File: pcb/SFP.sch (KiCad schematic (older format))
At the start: 13 parts

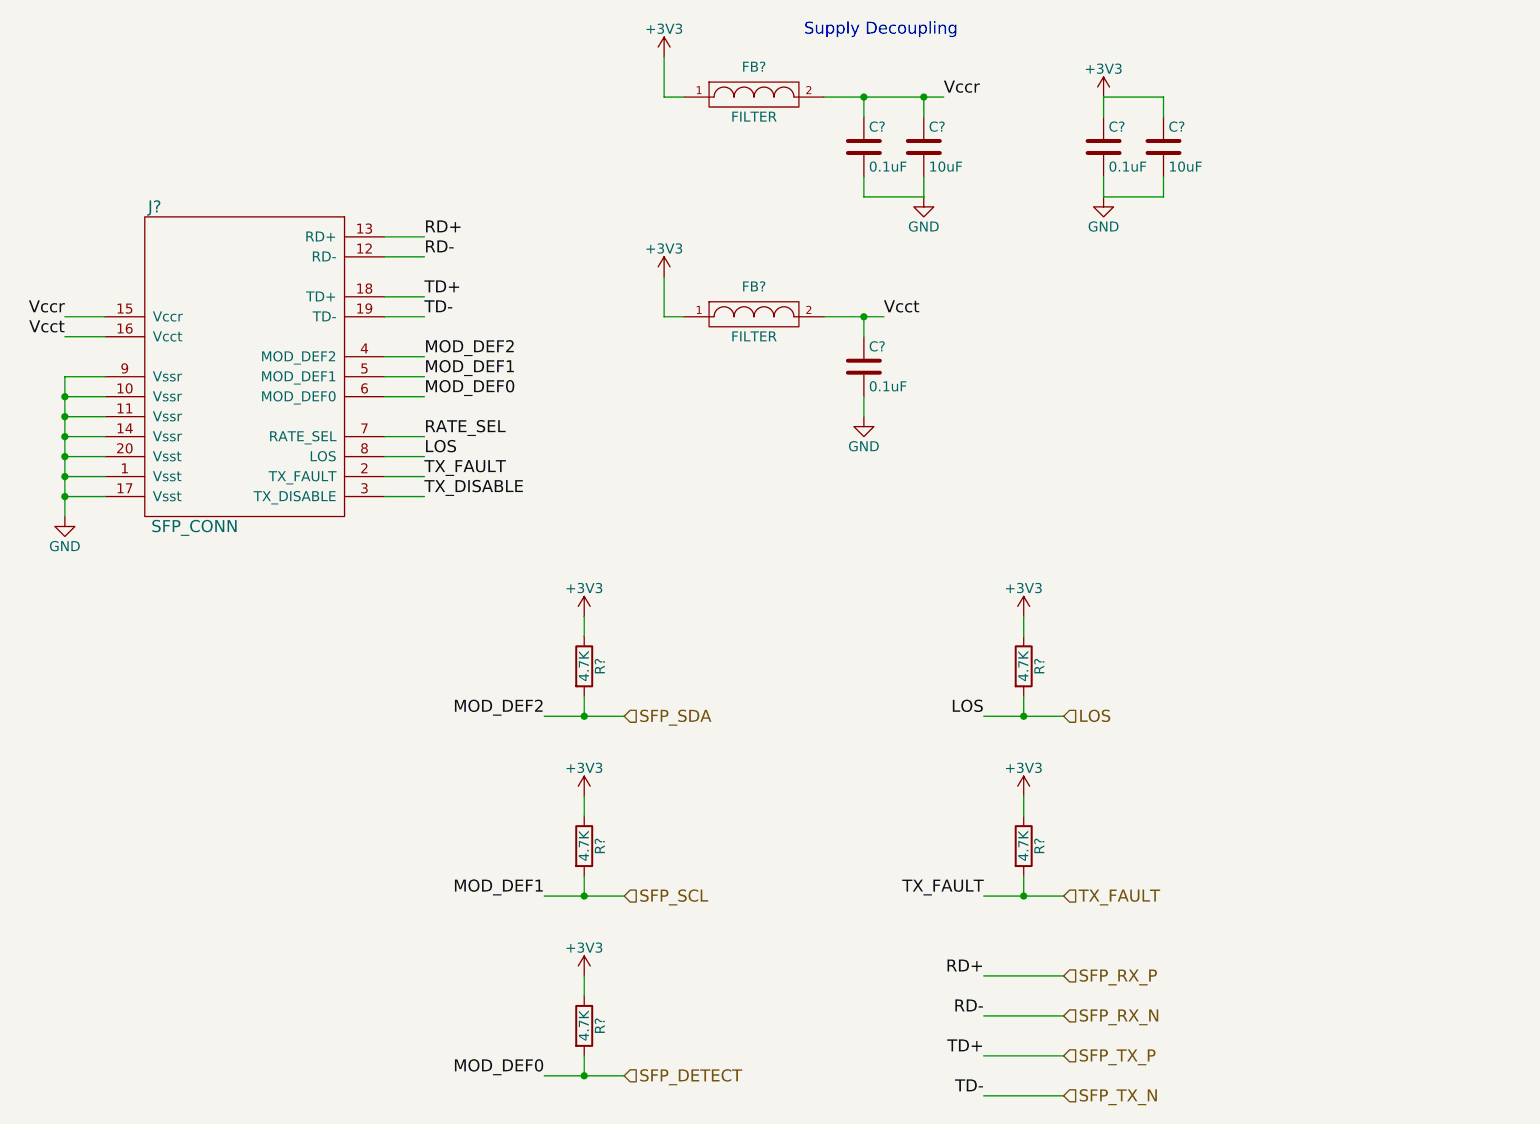
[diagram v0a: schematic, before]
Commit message: Added part numbers and updated schematic
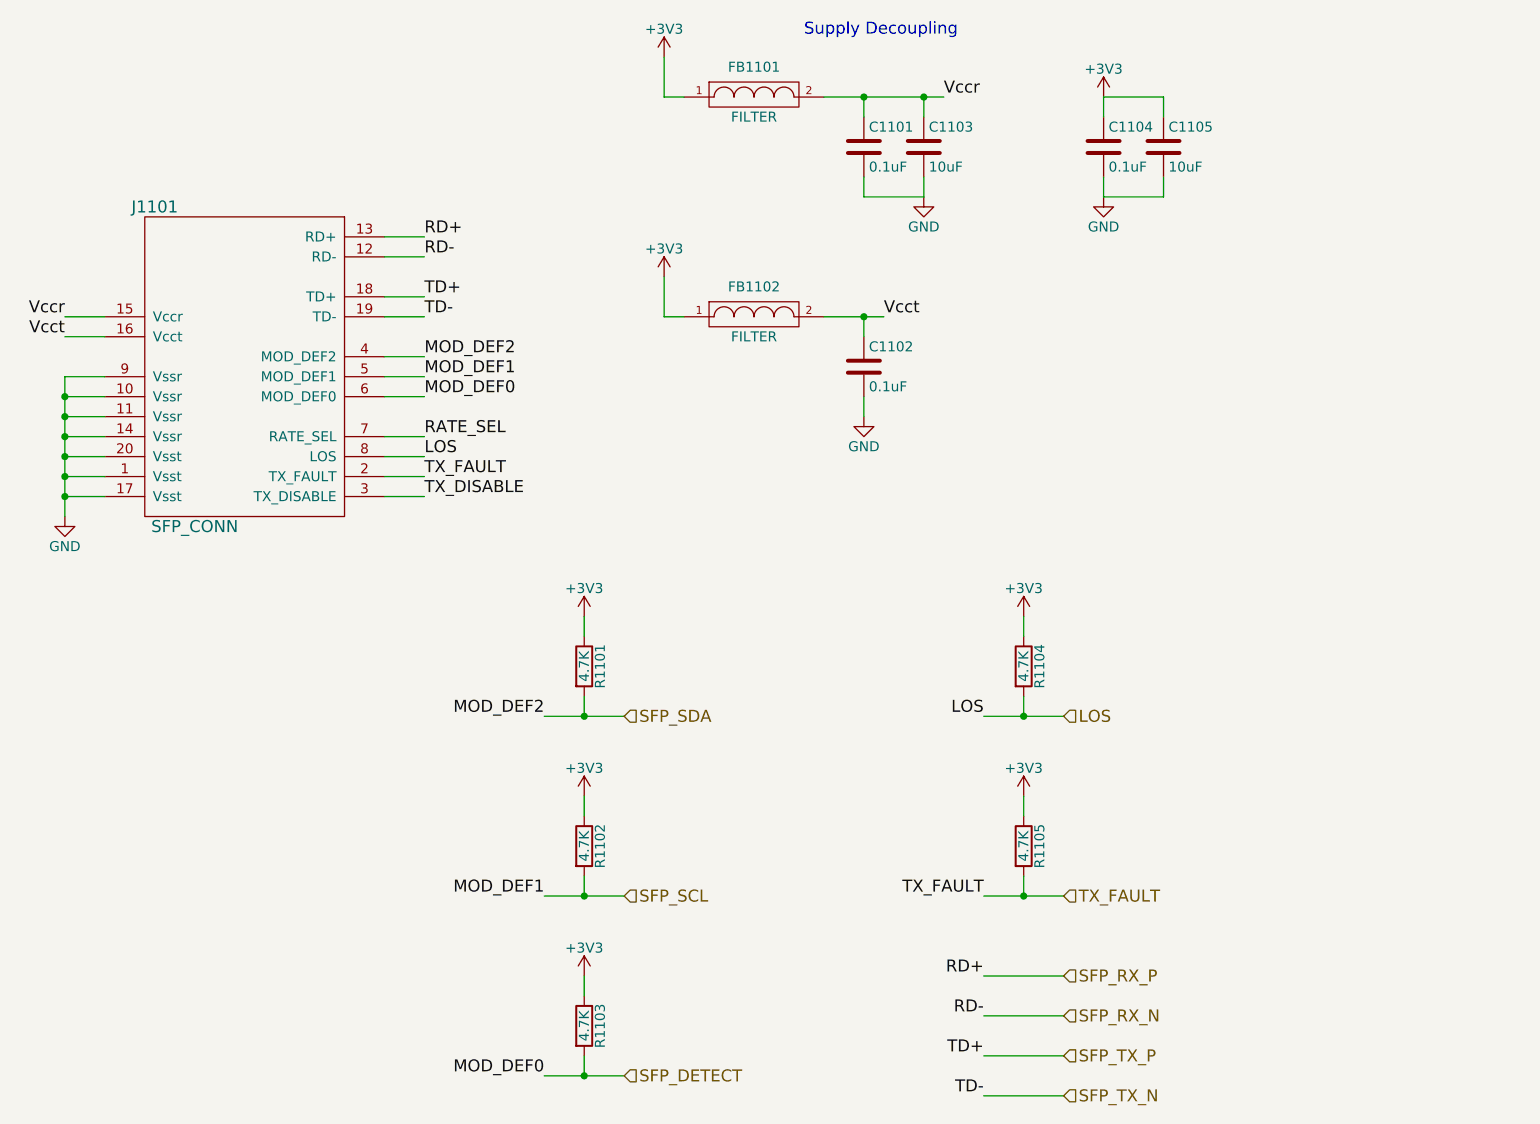
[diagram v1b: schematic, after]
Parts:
- gave numbers to parts that had none: 13
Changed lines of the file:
@@
 $EndDescr
 $Comp
-L SFP_CONN J?
+L SFP_CONN J1101
 U 1 1 56515F52
 P 3600 2350
-F 0 "J?" H 3150 3150 60  0000 C CNN
+F 0 "J1101" H 3150 3150 60  0000 C CNN
 F 1 "SFP_CONN" H 3350 1550 60  0000 C CNN
 F 2 "" H 5000 3150 60  0000 C CNN
@@
 $EndComp
 $Comp
-L GND #PWR?
+L GND #PWR1101
 U 1 1 56515F98
 P 2700 3100
-F 0 "#PWR?" H 2700 2850 50  0001 C CNN
+F 0 "#PWR1101" H 2700 2850 50  0001 C CNN
 F 1 "GND" H 2700 2950 50  0000 C CNN
 F 2 "" H 2700 3100 60  0000 C CNN
@@
 $EndComp
 $Comp
-L +3V3 #PWR?
+L +3V3 #PWR1111
 U 1 1 56515FAF
 P 7900 1000
-F 0 "#PWR?" H 7900 850 50  0001 C CNN
+F 0 "#PWR1111" H 7900 850 50  0001 C CNN
 F 1 "+3V3" H 7900 1140 50  0000 C CNN
 F 2 "" H 7900 1000 60  0000 C CNN
@@
 $EndComp
 $Comp
-L GND #PWR?
+L GND #PWR1112
 U 1 1 56515FCB
 P 7900 1500
-F 0 "#PWR?" H 7900 1250 50  0001 C CNN
+F 0 "#PWR1112" H 7900 1250 50  0001 C CNN
 F 1 "GND" H 7900 1350 50  0000 C CNN
 F 2 "" H 7900 1500 60  0000 C CNN
@@
 $EndComp
 $Comp
-L C C?
+L C C1104
 U 1 1 56515FE4
 P 7900 1250
-F 0 "C?" H 7925 1350 50  0000 L CNN
+F 0 "C1104" H 7925 1350 50  0000 L CNN
 F 1 "0.1uF" H 7925 1150 50  0000 L CNN
 F 2 "" H 7938 1100 30  0000 C CNN
@@
 $EndComp
 $Comp
-L C C?
+L C C1105
 U 1 1 5651600E
 P 8200 1250
-F 0 "C?" H 8225 1350 50  0000 L CNN
+F 0 "C1105" H 8225 1350 50  0000 L CNN
 F 1 "10uF" H 8225 1150 50  0000 L CNN
 F 2 "" H 8238 1100 30  0000 C CNN
@@
 $EndComp
 $Comp
-L C C?
+L C C1103
 U 1 1 56516041
 P 7000 1250
-F 0 "C?" H 7025 1350 50  0000 L CNN
+F 0 "C1103" H 7025 1350 50  0000 L CNN
 F 1 "10uF" H 7025 1150 50  0000 L CNN
 F 2 "" H 7038 1100 30  0000 C CNN
@@
 $EndComp
 $Comp
-L C C?
+L C C1101
 U 1 1 56516075
 P 6700 1250
-F 0 "C?" H 6725 1350 50  0000 L CNN
+F 0 "C1101" H 6725 1350 50  0000 L CNN
 F 1 "0.1uF" H 6725 1150 50  0000 L CNN
 F 2 "" H 6738 1100 30  0000 C CNN
@@
 $EndComp
 $Comp
-L C C?
+L C C1102
 U 1 1 5651609E
 P 6700 2350
-F 0 "C?" H 6725 2450 50  0000 L CNN
+F 0 "C1102" H 6725 2450 50  0000 L CNN
 F 1 "0.1uF" H 6725 2250 50  0000 L CNN
 F 2 "" H 6738 2200 30  0000 C CNN
@@
 $EndComp
 $Comp
-L FILTER FB?
+L FILTER FB1101
 U 1 1 565160D3
 P 6150 1000
-F 0 "FB?" H 6150 1150 50  0000 C CNN
+F 0 "FB1101" H 6150 1150 50  0000 C CNN
 F 1 "FILTER" H 6150 900 50  0000 C CNN
 F 2 "" H 6150 1000 60  0000 C CNN
@@
 $EndComp
 $Comp
-L FILTER FB?
+L FILTER FB1102
 U 1 1 5651610E
 P 6150 2100
-F 0 "FB?" H 6150 2250 50  0000 C CNN
+F 0 "FB1102" H 6150 2250 50  0000 C CNN
 F 1 "FILTER" H 6150 2000 50  0000 C CNN
 F 2 "" H 6150 2100 60  0000 C CNN
@@
 $EndComp
 $Comp
-L GND #PWR?
+L GND #PWR1108
 U 1 1 565162BE
 P 7000 1500
-F 0 "#PWR?" H 7000 1250 50  0001 C CNN
+F 0 "#PWR1108" H 7000 1250 50  0001 C CNN
 F 1 "GND" H 7000 1350 50  0000 C CNN
 F 2 "" H 7000 1500 60  0000 C CNN
@@
 $EndComp
 $Comp
-L GND #PWR?
+L GND #PWR1107
 U 1 1 5651631D
 P 6700 2600
-F 0 "#PWR?" H 6700 2350 50  0001 C CNN
+F 0 "#PWR1107" H 6700 2350 50  0001 C CNN
 F 1 "GND" H 6700 2450 50  0000 C CNN
 F 2 "" H 6700 2600 60  0000 C CNN
@@
 $EndComp
 $Comp
-L +3V3 #PWR?
+L +3V3 #PWR1105
 U 1 1 56516349
 P 5700 800
-F 0 "#PWR?" H 5700 650 50  0001 C CNN
+F 0 "#PWR1105" H 5700 650 50  0001 C CNN
 F 1 "+3V3" H 5700 940 50  0000 C CNN
 F 2 "" H 5700 800 60  0000 C CNN
@@
 $EndComp
 $Comp
-L +3V3 #PWR?
+L +3V3 #PWR1106
 U 1 1 56516375
 P 5700 1900
-F 0 "#PWR?" H 5700 1750 50  0001 C CNN
+F 0 "#PWR1106" H 5700 1750 50  0001 C CNN
 F 1 "+3V3" H 5700 2040 50  0000 C CNN
 F 2 "" H 5700 1900 60  0000 C CNN
@@
 TX_DISABLE
 $Comp
-L R R?
+L R R1104
 U 1 1 56516968
 P 7500 3850
-F 0 "R?" V 7580 3850 50  0000 C CNN
+F 0 "R1104" V 7580 3850 50  0000 C CNN
 F 1 "4.7K" V 7500 3850 50  0000 C CNN
 F 2 "" V 7430 3850 30  0000 C CNN
@@
 $EndComp
 $Comp
-L +3V3 #PWR?
+L +3V3 #PWR1109
 U 1 1 56516B32
 P 7500 3600
-F 0 "#PWR?" H 7500 3450 50  0001 C CNN
+F 0 "#PWR1109" H 7500 3450 50  0001 C CNN
 F 1 "+3V3" H 7500 3740 50  0000 C CNN
 F 2 "" H 7500 3600 60  0000 C CNN
@@
 Connection ~ 7500 4100
 $Comp
-L R R?
+L R R1105
 U 1 1 56516C87
 P 7500 4750
-F 0 "R?" V 7580 4750 50  0000 C CNN
+F 0 "R1105" V 7580 4750 50  0000 C CNN
 F 1 "4.7K" V 7500 4750 50  0000 C CNN
 F 2 "" V 7430 4750 30  0000 C CNN
@@
 $EndComp
 $Comp
-L +3V3 #PWR?
+L +3V3 #PWR1110
 U 1 1 56516C8D
 P 7500 4500
-F 0 "#PWR?" H 7500 4350 50  0001 C CNN
+F 0 "#PWR1110" H 7500 4350 50  0001 C CNN
 F 1 "+3V3" H 7500 4640 50  0000 C CNN
 F 2 "" H 7500 4500 60  0000 C CNN
@@
 Connection ~ 7500 5000
 $Comp
-L R R?
+L R R1101
 U 1 1 56516D0B
 P 5300 3850
-F 0 "R?" V 5380 3850 50  0000 C CNN
+F 0 "R1101" V 5380 3850 50  0000 C CNN
 F 1 "4.7K" V 5300 3850 50  0000 C CNN
 F 2 "" V 5230 3850 30  0000 C CNN
@@
 $EndComp
 $Comp
-L +3V3 #PWR?
+L +3V3 #PWR1102
 U 1 1 56516D11
 P 5300 3600
-F 0 "#PWR?" H 5300 3450 50  0001 C CNN
+F 0 "#PWR1102" H 5300 3450 50  0001 C CNN
 F 1 "+3V3" H 5300 3740 50  0000 C CNN
 F 2 "" H 5300 3600 60  0000 C CNN
@@
 Connection ~ 5300 4100
 $Comp
-L R R?
+L R R1102
 U 1 1 56516D1B
 P 5300 4750
-F 0 "R?" V 5380 4750 50  0000 C CNN
+F 0 "R1102" V 5380 4750 50  0000 C CNN
 F 1 "4.7K" V 5300 4750 50  0000 C CNN
 F 2 "" V 5230 4750 30  0000 C CNN
@@
 $EndComp
 $Comp
-L +3V3 #PWR?
+L +3V3 #PWR1103
 U 1 1 56516D21
 P 5300 4500
-F 0 "#PWR?" H 5300 4350 50  0001 C CNN
+F 0 "#PWR1103" H 5300 4350 50  0001 C CNN
 F 1 "+3V3" H 5300 4640 50  0000 C CNN
 F 2 "" H 5300 4500 60  0000 C CNN
@@
 MOD_DEF2
 $Comp
-L R R?
+L R R1103
 U 1 1 56516D9A
 P 5300 5650
-F 0 "R?" V 5380 5650 50  0000 C CNN
+F 0 "R1103" V 5380 5650 50  0000 C CNN
 F 1 "4.7K" V 5300 5650 50  0000 C CNN
 F 2 "" V 5230 5650 30  0000 C CNN
@@
 $EndComp
 $Comp
-L +3V3 #PWR?
+L +3V3 #PWR1104
 U 1 1 56516DA0
 P 5300 5400
-F 0 "#PWR?" H 5300 5250 50  0001 C CNN
+F 0 "#PWR1104" H 5300 5250 50  0001 C CNN
 F 1 "+3V3" H 5300 5540 50  0000 C CNN
 F 2 "" H 5300 5400 60  0000 C CNN

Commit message: mostly done with component placement
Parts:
- C1101, C1102, C1103, C1104, C1105: footprint (none) -> wbraun_smd:C_0402
- FB1101, FB1102: footprint (none) -> wbraun_smd:L_0603
- J1101: footprint (none) -> wbraun_smd:CONN-SFP_1367073-1
- R1101, R1102, R1103, R1104, R1105: footprint (none) -> wbraun_smd:R_0402
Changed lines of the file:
@@
 F 0 "J1101" H 3150 3150 60  0000 C CNN
 F 1 "SFP_CONN" H 3350 1550 60  0000 C CNN
-F 2 "" H 5000 3150 60  0000 C CNN
+F 2 "wbraun_smd:CONN-SFP_1367073-1" H 5000 3150 60  0001 C CNN
 F 3 "" H 5000 3150 60  0000 C CNN
 	1    3600 2350
@@
 $EndComp
 $Comp
-L GND #PWR1101
+L GND #PWR0153
 U 1 1 56515F98
 P 2700 3100
-F 0 "#PWR1101" H 2700 2850 50  0001 C CNN
+F 0 "#PWR0153" H 2700 2850 50  0001 C CNN
 F 1 "GND" H 2700 2950 50  0000 C CNN
 F 2 "" H 2700 3100 60  0000 C CNN
@@
 $EndComp
 $Comp
-L +3V3 #PWR1111
+L +3V3 #PWR0154
 U 1 1 56515FAF
 P 7900 1000
-F 0 "#PWR1111" H 7900 850 50  0001 C CNN
+F 0 "#PWR0154" H 7900 850 50  0001 C CNN
 F 1 "+3V3" H 7900 1140 50  0000 C CNN
 F 2 "" H 7900 1000 60  0000 C CNN
@@
 $EndComp
 $Comp
-L GND #PWR1112
+L GND #PWR0155
 U 1 1 56515FCB
 P 7900 1500
-F 0 "#PWR1112" H 7900 1250 50  0001 C CNN
+F 0 "#PWR0155" H 7900 1250 50  0001 C CNN
 F 1 "GND" H 7900 1350 50  0000 C CNN
 F 2 "" H 7900 1500 60  0000 C CNN
@@
 F 0 "C1104" H 7925 1350 50  0000 L CNN
 F 1 "0.1uF" H 7925 1150 50  0000 L CNN
-F 2 "" H 7938 1100 30  0000 C CNN
+F 2 "wbraun_smd:C_0402" H 7938 1100 30  0001 C CNN
 F 3 "" H 7900 1250 60  0000 C CNN
 	1    7900 1250
@@
 F 0 "C1105" H 8225 1350 50  0000 L CNN
 F 1 "10uF" H 8225 1150 50  0000 L CNN
-F 2 "" H 8238 1100 30  0000 C CNN
+F 2 "wbraun_smd:C_0402" H 8238 1100 30  0001 C CNN
 F 3 "" H 8200 1250 60  0000 C CNN
 	1    8200 1250
@@
 F 0 "C1103" H 7025 1350 50  0000 L CNN
 F 1 "10uF" H 7025 1150 50  0000 L CNN
-F 2 "" H 7038 1100 30  0000 C CNN
+F 2 "wbraun_smd:C_0402" H 7038 1100 30  0001 C CNN
 F 3 "" H 7000 1250 60  0000 C CNN
 	1    7000 1250
@@
 F 0 "C1101" H 6725 1350 50  0000 L CNN
 F 1 "0.1uF" H 6725 1150 50  0000 L CNN
-F 2 "" H 6738 1100 30  0000 C CNN
+F 2 "wbraun_smd:C_0402" H 6738 1100 30  0001 C CNN
 F 3 "" H 6700 1250 60  0000 C CNN
 	1    6700 1250
@@
 F 0 "C1102" H 6725 2450 50  0000 L CNN
 F 1 "0.1uF" H 6725 2250 50  0000 L CNN
-F 2 "" H 6738 2200 30  0000 C CNN
+F 2 "wbraun_smd:C_0402" H 6738 2200 30  0001 C CNN
 F 3 "" H 6700 2350 60  0000 C CNN
 	1    6700 2350
@@
 F 0 "FB1101" H 6150 1150 50  0000 C CNN
 F 1 "FILTER" H 6150 900 50  0000 C CNN
-F 2 "" H 6150 1000 60  0000 C CNN
+F 2 "wbraun_smd:L_0603" H 6150 1000 60  0001 C CNN
 F 3 "" H 6150 1000 60  0000 C CNN
 	1    6150 1000
@@
 F 0 "FB1102" H 6150 2250 50  0000 C CNN
 F 1 "FILTER" H 6150 2000 50  0000 C CNN
-F 2 "" H 6150 2100 60  0000 C CNN
+F 2 "wbraun_smd:L_0603" H 6150 2100 60  0001 C CNN
 F 3 "" H 6150 2100 60  0000 C CNN
 	1    6150 2100
@@
 $EndComp
 $Comp
-L GND #PWR1108
+L GND #PWR0156
 U 1 1 565162BE
 P 7000 1500
-F 0 "#PWR1108" H 7000 1250 50  0001 C CNN
+F 0 "#PWR0156" H 7000 1250 50  0001 C CNN
 F 1 "GND" H 7000 1350 50  0000 C CNN
 F 2 "" H 7000 1500 60  0000 C CNN
@@
 $EndComp
 $Comp
-L GND #PWR1107
+L GND #PWR0157
 U 1 1 5651631D
 P 6700 2600
-F 0 "#PWR1107" H 6700 2350 50  0001 C CNN
+F 0 "#PWR0157" H 6700 2350 50  0001 C CNN
 F 1 "GND" H 6700 2450 50  0000 C CNN
 F 2 "" H 6700 2600 60  0000 C CNN
@@
 $EndComp
 $Comp
-L +3V3 #PWR1105
+L +3V3 #PWR0158
 U 1 1 56516349
 P 5700 800
-F 0 "#PWR1105" H 5700 650 50  0001 C CNN
+F 0 "#PWR0158" H 5700 650 50  0001 C CNN
 F 1 "+3V3" H 5700 940 50  0000 C CNN
 F 2 "" H 5700 800 60  0000 C CNN
@@
 $EndComp
 $Comp
-L +3V3 #PWR1106
+L +3V3 #PWR0159
 U 1 1 56516375
 P 5700 1900
-F 0 "#PWR1106" H 5700 1750 50  0001 C CNN
+F 0 "#PWR0159" H 5700 1750 50  0001 C CNN
 F 1 "+3V3" H 5700 2040 50  0000 C CNN
 F 2 "" H 5700 1900 60  0000 C CNN
@@
 F 0 "R1104" V 7580 3850 50  0000 C CNN
 F 1 "4.7K" V 7500 3850 50  0000 C CNN
-F 2 "" V 7430 3850 30  0000 C CNN
+F 2 "wbraun_smd:R_0402" V 7430 3850 30  0001 C CNN
 F 3 "" H 7500 3850 30  0000 C CNN
 	1    7500 3850
@@
 $EndComp
 $Comp
-L +3V3 #PWR1109
+L +3V3 #PWR0160
 U 1 1 56516B32
 P 7500 3600
-F 0 "#PWR1109" H 7500 3450 50  0001 C CNN
+F 0 "#PWR0160" H 7500 3450 50  0001 C CNN
 F 1 "+3V3" H 7500 3740 50  0000 C CNN
 F 2 "" H 7500 3600 60  0000 C CNN
@@
 F 0 "R1105" V 7580 4750 50  0000 C CNN
 F 1 "4.7K" V 7500 4750 50  0000 C CNN
-F 2 "" V 7430 4750 30  0000 C CNN
+F 2 "wbraun_smd:R_0402" V 7430 4750 30  0001 C CNN
 F 3 "" H 7500 4750 30  0000 C CNN
 	1    7500 4750
@@
 $EndComp
 $Comp
-L +3V3 #PWR1110
+L +3V3 #PWR0161
 U 1 1 56516C8D
 P 7500 4500
-F 0 "#PWR1110" H 7500 4350 50  0001 C CNN
+F 0 "#PWR0161" H 7500 4350 50  0001 C CNN
 F 1 "+3V3" H 7500 4640 50  0000 C CNN
 F 2 "" H 7500 4500 60  0000 C CNN
@@
 F 0 "R1101" V 5380 3850 50  0000 C CNN
 F 1 "4.7K" V 5300 3850 50  0000 C CNN
-F 2 "" V 5230 3850 30  0000 C CNN
+F 2 "wbraun_smd:R_0402" V 5230 3850 30  0001 C CNN
 F 3 "" H 5300 3850 30  0000 C CNN
 	1    5300 3850
@@
 $EndComp
 $Comp
-L +3V3 #PWR1102
+L +3V3 #PWR0162
 U 1 1 56516D11
 P 5300 3600
-F 0 "#PWR1102" H 5300 3450 50  0001 C CNN
+F 0 "#PWR0162" H 5300 3450 50  0001 C CNN
 F 1 "+3V3" H 5300 3740 50  0000 C CNN
 F 2 "" H 5300 3600 60  0000 C CNN
@@
 F 0 "R1102" V 5380 4750 50  0000 C CNN
 F 1 "4.7K" V 5300 4750 50  0000 C CNN
-F 2 "" V 5230 4750 30  0000 C CNN
+F 2 "wbraun_smd:R_0402" V 5230 4750 30  0001 C CNN
 F 3 "" H 5300 4750 30  0000 C CNN
 	1    5300 4750
@@
 $EndComp
 $Comp
-L +3V3 #PWR1103
+L +3V3 #PWR0163
 U 1 1 56516D21
 P 5300 4500
-F 0 "#PWR1103" H 5300 4350 50  0001 C CNN
+F 0 "#PWR0163" H 5300 4350 50  0001 C CNN
 F 1 "+3V3" H 5300 4640 50  0000 C CNN
 F 2 "" H 5300 4500 60  0000 C CNN
@@
 F 0 "R1103" V 5380 5650 50  0000 C CNN
 F 1 "4.7K" V 5300 5650 50  0000 C CNN
-F 2 "" V 5230 5650 30  0000 C CNN
+F 2 "wbraun_smd:R_0402" V 5230 5650 30  0001 C CNN
 F 3 "" H 5300 5650 30  0000 C CNN
 	1    5300 5650
@@
 $EndComp
 $Comp
-L +3V3 #PWR1104
+L +3V3 #PWR0164
 U 1 1 56516DA0
 P 5300 5400
-F 0 "#PWR1104" H 5300 5250 50  0001 C CNN
+F 0 "#PWR0164" H 5300 5250 50  0001 C CNN
 F 1 "+3V3" H 5300 5540 50  0000 C CNN
 F 2 "" H 5300 5400 60  0000 C CNN
